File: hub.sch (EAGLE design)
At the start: 27 parts, among them U1 10118194-MICRO-USB, U2 LM3671MF-3.3/NOPBMF05A-M, U3 SN74LVC1T45DBVRDBV6-M, U4 SN74LVC1T45DBVRDBV6-M

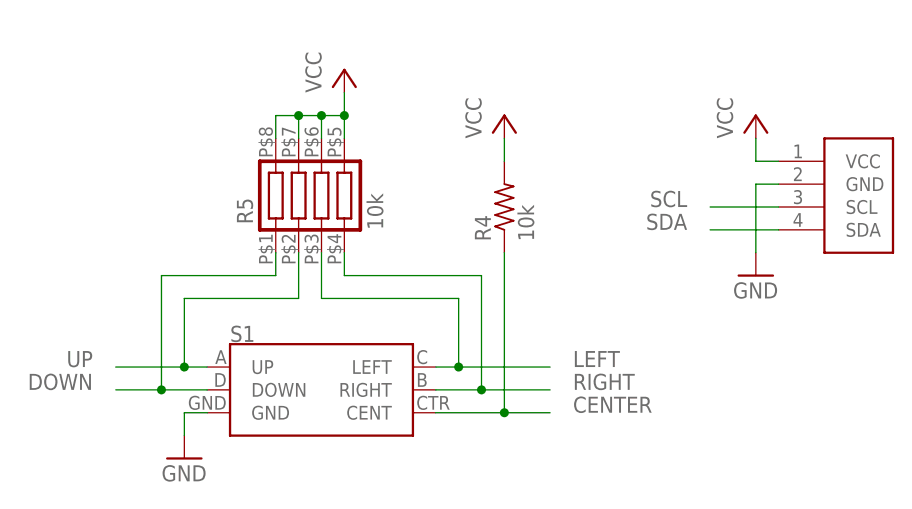
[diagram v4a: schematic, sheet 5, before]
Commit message: Wired up lots of support circuitry
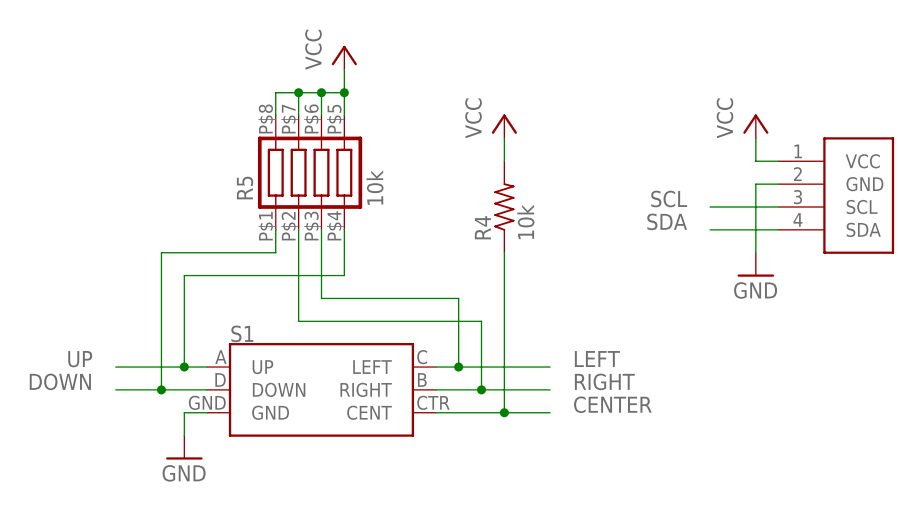
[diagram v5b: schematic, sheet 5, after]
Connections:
- removed net GPIO4: JP7.6, U$2.IO4
- net +5V: now also JP7.2
- net CENTER: now also U$2.IO4
- net DOWN: now also U$2.IO5
- net GPIO17: now also JP7.6; no longer JP7.2
- net LEFT: now also U$2.IO35
- net RIGHT: now also R5.2, U$2.IO34; no longer R5.4
- net UP: now also R5.4, U$2.IO19; no longer R5.2
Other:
- moved on the sheet: R5

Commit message: Finished layout!
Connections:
- net TCK: now also JP3.3; no longer JP3.4
- net TDI: now also JP3.4; no longer JP3.3
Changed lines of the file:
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@@
 </segment>
 </net>
-<net name="TDI" class="0">
+<net name="TCK" class="0">
 <segment>
 <pinref part="JP3" gate="A" pin="3"/>
 <wire x1="66.04" y1="66.04" x2="55.88" y2="66.04" width="0.1524" layer="91"/>
 <label x="53.34" y="66.04" size="1.778" layer="95" align="bottom-right"/>
-</segment>
-</net>
-<net name="TCK" class="0">
-<segment>
-<pinref part="JP3" gate="A" pin="4"/>
-<wire x1="73.66" y1="66.04" x2="86.36" y2="66.04" width="0.1524" layer="91"/>
-<label x="88.9" y="66.04" size="1.778" layer="95"/>
 </segment>
 </net>
@@
 </segment>
 </net>
+<net name="TDI" class="0">
+<segment>
+<pinref part="JP3" gate="A" pin="4"/>
+<wire x1="73.66" y1="66.04" x2="86.36" y2="66.04" width="0.1524" layer="91"/>
+<label x="88.9" y="66.04" size="1.778" layer="95"/>
+</segment>
+</net>

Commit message: Final tweaks and BOM creation
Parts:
- renumbered U$1 to U5, U$4 to U6
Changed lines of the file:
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@@
 <part name="R1" library="rcl" library_urn="urn:adsk.eagle:library:334" deviceset="R-US_" device="R0805" package3d_urn="urn:adsk.eagle:package:23553/2" value="10k"/>
 <part name="R2" library="rcl" library_urn="urn:adsk.eagle:library:334" deviceset="R-US_" device="R0805" package3d_urn="urn:adsk.eagle:package:23553/2" value="10k"/>
-<part name="U$1" library="nebrius" deviceset="SS8050-G" device=""/>
-<part name="U$4" library="nebrius" deviceset="SS8050-G" device=""/>
+<part name="U5" library="nebrius" deviceset="SS8050-G" device=""/>
+<part name="U6" library="nebrius" deviceset="SS8050-G" device=""/>
 <part name="S1" library="SparkFun-Switches" library_urn="urn:adsk.eagle:library:535" deviceset="JOYSTICK_MINI" device="" package3d_urn="urn:adsk.eagle:package:40157/1"/>
 <part name="R3" library="rcl" library_urn="urn:adsk.eagle:library:334" deviceset="R-US_" device="R0805" package3d_urn="urn:adsk.eagle:package:23553/2" value="10k"/>
@@
 <attribute name="VALUE" x="36.83" y="37.338" size="1.778" layer="96"/>
 </instance>
-<instance part="U$1" gate="G$1" x="30.48" y="58.42" smashed="yes" rot="MR0">
+<instance part="U5" gate="G$1" x="30.48" y="58.42" smashed="yes" rot="MR0">
 <attribute name="NAME" x="25.4" y="58.42" size="1.778" layer="95" rot="MR0"/>
 <attribute name="VALUE" x="25.4" y="55.88" size="1.778" layer="96" rot="MR0"/>
 </instance>
-<instance part="U$4" gate="G$1" x="30.48" y="40.64" smashed="yes" rot="R180">
+<instance part="U6" gate="G$1" x="30.48" y="40.64" smashed="yes" rot="R180">
 <attribute name="NAME" x="25.4" y="40.64" size="1.778" layer="95" rot="R180"/>
 <attribute name="VALUE" x="25.4" y="43.18" size="1.778" layer="96" rot="R180"/>
@@
 <net name="N$4" class="0">
 <segment>
-<pinref part="U$1" gate="G$1" pin="B"/>
+<pinref part="U5" gate="G$1" pin="B"/>
 <pinref part="R1" gate="G$1" pin="1"/>
 <wire x1="33.02" y1="58.42" x2="35.56" y2="58.42" width="0.1524" layer="91"/>
@@
 <pinref part="R2" gate="G$1" pin="2"/>
 <wire x1="45.72" y1="40.64" x2="48.26" y2="40.64" width="0.1524" layer="91"/>
-<pinref part="U$1" gate="G$1" pin="E"/>
+<pinref part="U5" gate="G$1" pin="E"/>
 <wire x1="27.94" y1="53.34" x2="27.94" y2="50.8" width="0.1524" layer="91"/>
 <wire x1="27.94" y1="50.8" x2="48.26" y2="50.8" width="0.1524" layer="91"/>
@@
 <wire x1="50.8" y1="48.26" x2="50.8" y2="58.42" width="0.1524" layer="91"/>
 <junction x="50.8" y="58.42"/>
-<pinref part="U$4" gate="G$1" pin="E"/>
+<pinref part="U6" gate="G$1" pin="E"/>
 <wire x1="27.94" y1="48.26" x2="27.94" y2="45.72" width="0.1524" layer="91"/>
 <wire x1="50.8" y1="58.42" x2="55.88" y2="58.42" width="0.1524" layer="91"/>
@@
 <net name="N$5" class="0">
 <segment>
-<pinref part="U$4" gate="G$1" pin="B"/>
+<pinref part="U6" gate="G$1" pin="B"/>
 <pinref part="R2" gate="G$1" pin="1"/>
 <wire x1="33.02" y1="40.64" x2="35.56" y2="40.64" width="0.1524" layer="91"/>
@@
 <net name="IO0" class="0">
 <segment>
-<pinref part="U$4" gate="G$1" pin="C"/>
+<pinref part="U6" gate="G$1" pin="C"/>
 <wire x1="27.94" y1="35.56" x2="27.94" y2="33.02" width="0.1524" layer="91"/>
 <label x="20.32" y="33.02" size="1.778" layer="95" align="bottom-right"/>
@@
 <net name="EN" class="0">
 <segment>
-<pinref part="U$1" gate="G$1" pin="C"/>
+<pinref part="U5" gate="G$1" pin="C"/>
 <label x="20.32" y="66.04" size="1.778" layer="95" align="bottom-right"/>
 <wire x1="27.94" y1="63.5" x2="27.94" y2="66.04" width="0.1524" layer="91"/>
